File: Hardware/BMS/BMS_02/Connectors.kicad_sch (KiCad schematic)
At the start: 25 parts, among them J1 Conn_01x07, J10 7807, J11 Conn_01x04, J12 Conn_01x02, J13 Conn_01x06, J14 USB_B_Micro, J15 Conn_01x02, J16 Conn_01x02, J17 7807, J18 7807, J19 7807, J2 Conn_01x06, J20 Conn_01x02, J3 Conn_01x06, J4 Conn_01x06, J5 Conn_02x06_Odd_Even, J6 Conn_02x06_Odd_Even, J7 Conn_02x06_Odd_Even, J8 Conn_02x06_Odd_Even, J9 Conn_01x04

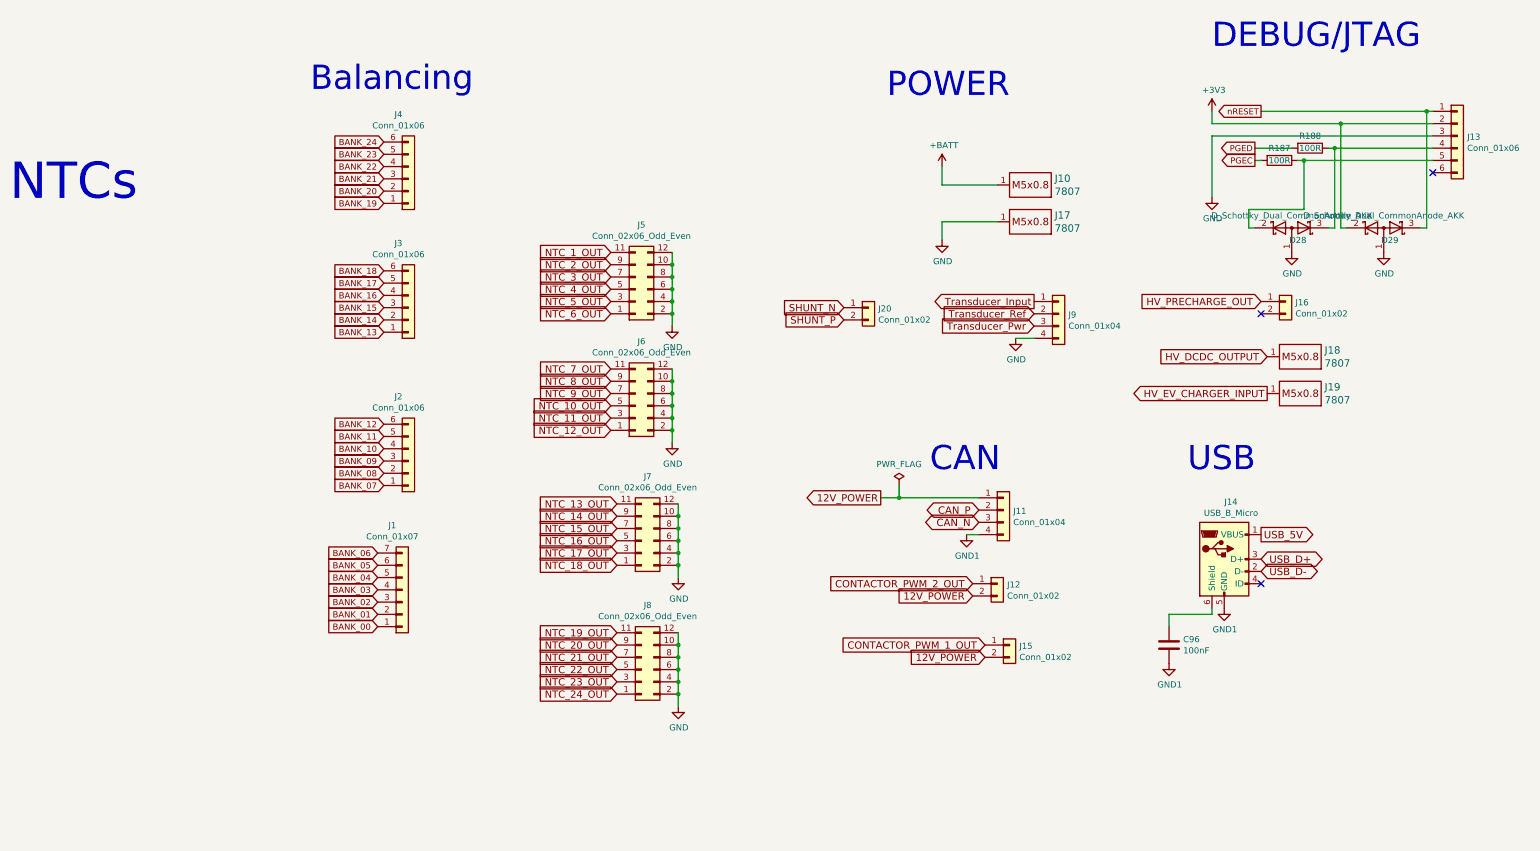
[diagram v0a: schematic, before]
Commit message: bms 02 build and code bring up. Board is built, bootloader is stable and uploads app flawlessly.
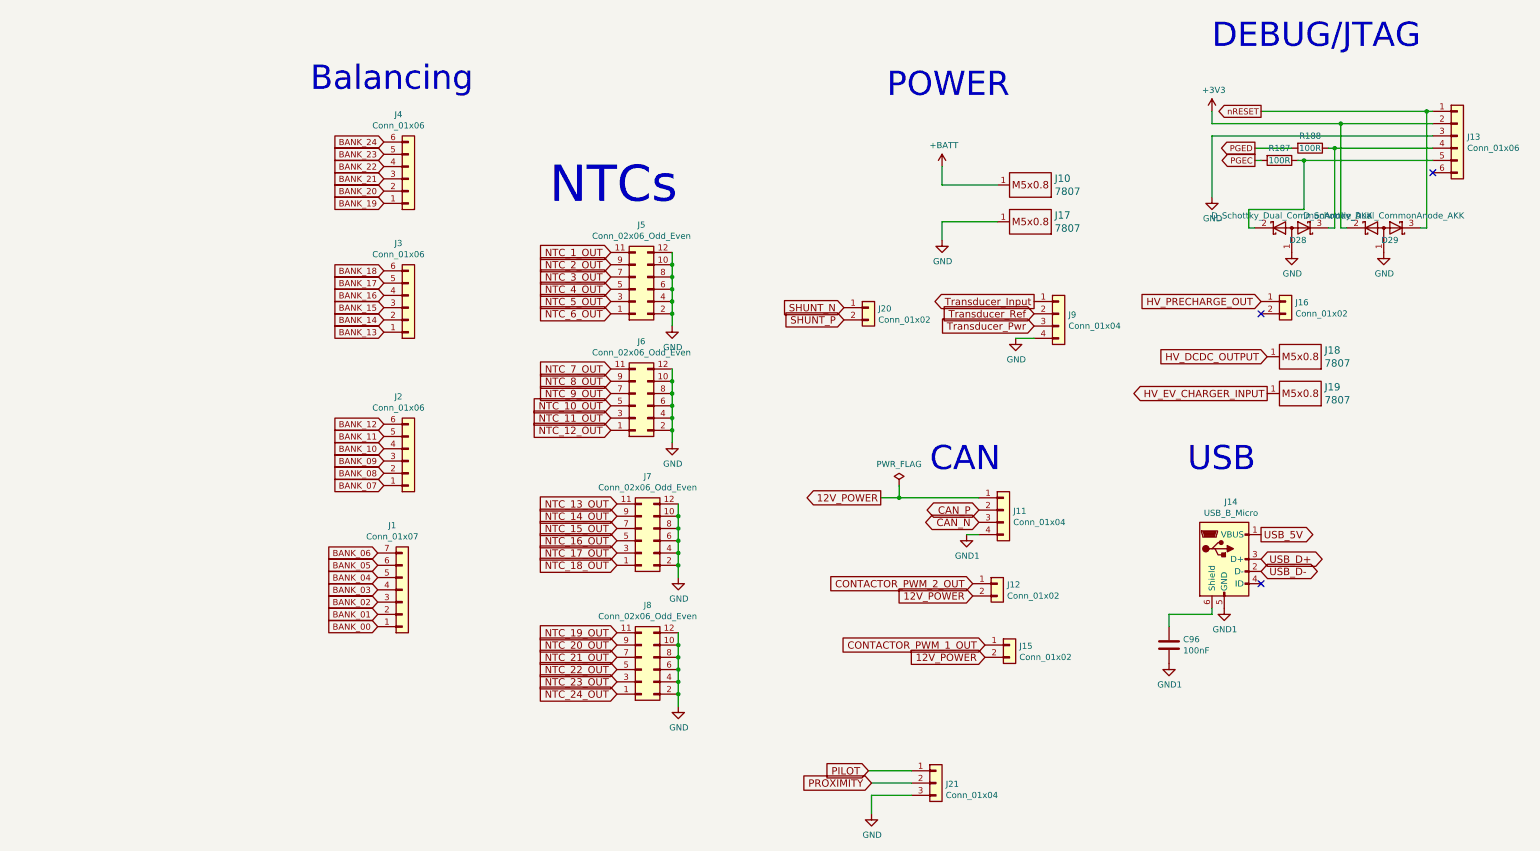
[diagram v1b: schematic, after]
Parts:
- added J21: Conn_01x04, Connector_JST:JST_XH_B3B-XH-A_1x03_P2.50mm_Vertical, symbol Connector_Generic:Conn_01x03
- C96, J13, R187, R188: DNP (none) -> (none)
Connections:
- net GND: now also J21.3 (Pin_3)
- new net PILOT: J21.1 (Pin_1)
- new net PROXIMITY: J21.2 (Pin_2)
